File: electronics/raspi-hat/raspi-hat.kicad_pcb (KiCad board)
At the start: 0 parts

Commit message: Start laying out PCB for raspberry pi hat
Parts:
- added C1: 4.7uF, Capacitor_SMD:C_0603_1608Metric, F.Cu at (123.4, 21.1)
- added C10: 15pF, Capacitor_SMD:C_0603_1608Metric, F.Cu at (29.7, 71.3)
- added C2: 4.7uF, Capacitor_SMD:C_0603_1608Metric, F.Cu at (127.5, 21.1)
- added C3: 4.7uF, Capacitor_SMD:C_0603_1608Metric, F.Cu at (105.8, 47.5)
- added C4: 4.7uF, Capacitor_SMD:C_0603_1608Metric, F.Cu at (123.4, 23.6)
- added C5: 4.7uF, Capacitor_SMD:C_0603_1608Metric, F.Cu at (116.3, 39.4)
- added C6: HHXB350ARA680MF80G, Capacitor_SMD:CP_Elec_6.3x7.7, F.Cu at (186.2, 112.6)
- added C7: 10μF, Capacitor_SMD:C_0603_1608Metric, F.Cu at (71.4, 41.1)
- added C8: 22μF, Capacitor_SMD:C_0603_1608Metric, F.Cu at (71.4, 43.7)
- added C9: 15pF, Capacitor_SMD:C_0603_1608Metric, F.Cu at (38.2, 62.6)
- added J1: Raspberry Pi 40-Pin, Connector_PinHeader_2.54mm:PinHeader_2x20_P2.54mm_Vertical, F.Cu at (137.2, 83.8)
- added J2: 24V, Custom Footprints:PowerPoleThroughHole, F.Cu at (188.0, 82.0)
- added J3: 12V to other boards, Custom Footprints:PowerPoleThroughHole, F.Cu at (170.2, 82.0)
- added J4: CAN, Custom Footprints:LatchingConnector2POS, F.Cu at (141.0, 76.6)
- added J5: 5V to other boards, Custom Footprints:LatchingConnector2POS, F.Cu at (151.1, 76.4)
- added Q1: DMG2305UX-13, digikey-footprints:SOT-23-3, F.Cu at (35.3, 67.9)
- added R1: 10kΩ, Resistor_SMD:R_0603_1608Metric, F.Cu at (82.8, 60.7)
- added R10: 10k, Resistor_SMD:R_0603_1608Metric, F.Cu at (38.2, 60.1)
- added R2: 47kΩ, Resistor_SMD:R_0603_1608Metric, F.Cu at (71.4, 50.1)
- added R3: 330kΩ, Resistor_SMD:R_0603_1608Metric, F.Cu at (84.9, 43.7)
- added R4: 18kΩ, Resistor_SMD:R_0603_1608Metric, F.Cu at (84.9, 41.1)
- added R5: 3kΩ, Resistor_SMD:R_0603_1608Metric, F.Cu at (88.9, 41.1)
- added R6: 68Ω, Resistor_SMD:R_0603_1608Metric, F.Cu at (88.9, 43.7)
- added R7: 510kΩ, Resistor_SMD:R_0603_1608Metric, F.Cu at (75.4, 41.1)
- added R8: 100k, Resistor_SMD:R_0603_1608Metric, F.Cu at (137.3, 34.3)
- added R9: 150Ω, Resistor_SMD:R_0603_1608Metric, F.Cu at (150.0, 21.1)
- added U1: MCP2515-xSO, Package_SO:SOIC-18W_7.5x11.6mm_P1.27mm, F.Cu at (152.4, 101.6)
- added U2: MAX33012EASA+, MAX33012EASA+:MAX33012EASA+, F.Cu at (147.3, 86.4)
- added U3: DMMT5401-7-F, DMMT5401-7-F:DMMT5401-7-F, F.Cu at (121.9, 78.7)
- added U4: MYSGK02506BRSR, MYSGK02506BRSR:Murata-MYSGK-06-0-0-MFG, F.Cu at (186.7, 99.1)
- added U5: MYMGA5R04RELA5RA, MYMGA5R04RELA5RA:MYMGA5R04RELA5RA, F.Cu at (168.9, 96.5)
- added Y1: Crystal_GND24_Small, Crystal:Crystal_SMD_3225-4Pin_3.2x2.5mm, F.Cu at (58.9, 52.5)
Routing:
- net Net-(U1-Pad1): track 0.00 -> 23.3 mm
- net /SCLK: track 0.00 -> 23.0 mm, vias 0 -> 1
- net Net-(U1-Pad2): track 0.00 -> 20.4 mm
- net /CS: track 0.00 -> 17.8 mm
- net /INT: track 0.00 -> 17.5 mm, vias 0 -> 1
- net /SDO: track 0.00 -> 13.2 mm
- net /SDI: track 0.00 -> 12.7 mm
- net Net-(J4-Pad1): track 0.00 -> 9.64 mm
- net Net-(J4-Pad2): track 0.00 -> 9.12 mm
- added copper zone on F.Cu, net GND
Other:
- copper layers 0 -> 4

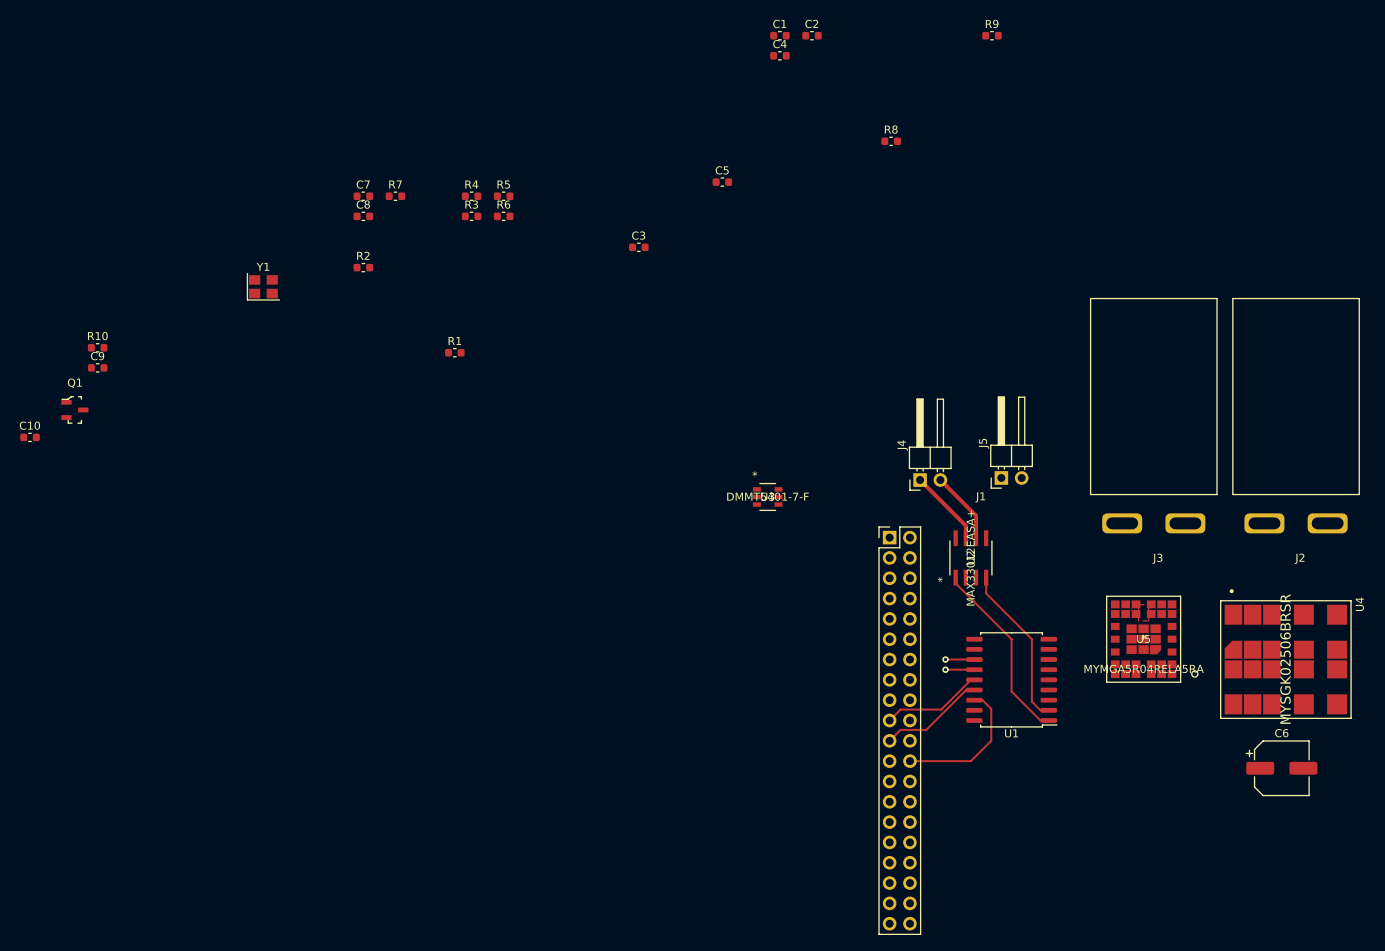
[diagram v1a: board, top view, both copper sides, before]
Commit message: Finish designing raspi hat
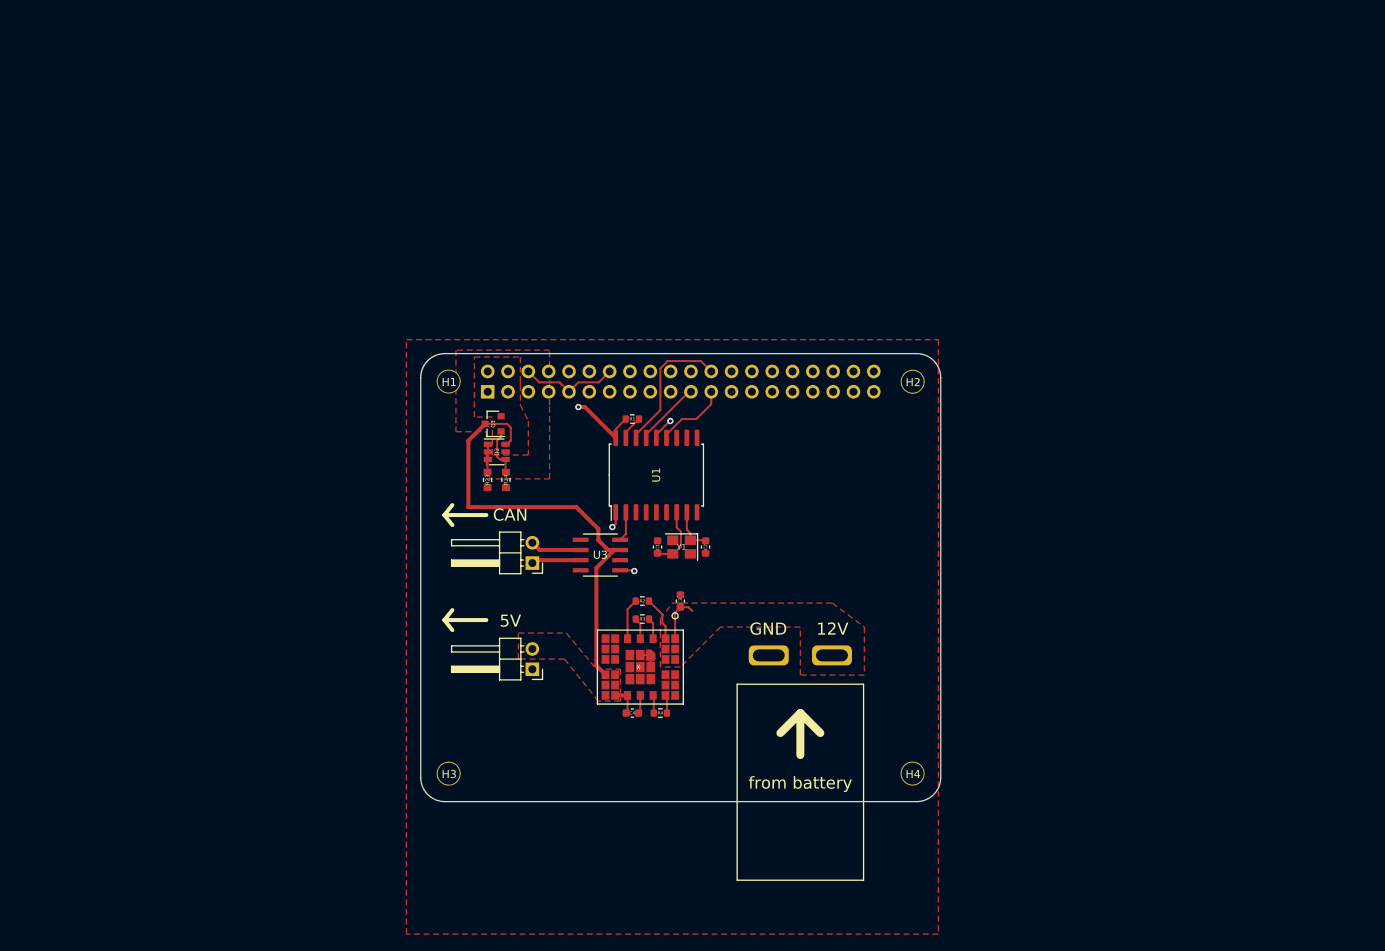
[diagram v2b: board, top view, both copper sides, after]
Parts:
- removed C10, C9: 15pF, Capacitor_SMD:C_0603_1608Metric
- removed C5: 4.7uF, Capacitor_SMD:C_0603_1608Metric
- removed C6: HHXB350ARA680MF80G, Capacitor_SMD:CP_Elec_6.3x7.7
- removed C7: 10μF, Capacitor_SMD:C_0603_1608Metric
- removed C8: 22μF, Capacitor_SMD:C_0603_1608Metric
- removed J5: 5V to other boards, Custom Footprints:LatchingConnector2POS
- removed R10: 10k, Resistor_SMD:R_0603_1608Metric
- removed R5: 3kΩ, Resistor_SMD:R_0603_1608Metric
- removed R6: 68Ω, Resistor_SMD:R_0603_1608Metric
- removed R7: 510kΩ, Resistor_SMD:R_0603_1608Metric
- removed R8: 100k, Resistor_SMD:R_0603_1608Metric
- removed R9: 150Ω, Resistor_SMD:R_0603_1608Metric
- removed U2: MAX33012EASA+, MAX33012EASA+:MAX33012EASA+
- removed U5: MYMGA5R04RELA5RA, MYMGA5R04RELA5RA:MYMGA5R04RELA5RA
- added H1: 3mm_Mounting_Hole, project_footprints:NPTH_3mm_ID, F.Cu at (82.0, 64.3)
- added H2: 3mm_Mounting_Hole, project_footprints:NPTH_3mm_ID, F.Cu at (140.0, 64.3)
- added H3: 3mm_Mounting_Hole, project_footprints:NPTH_3mm_ID, F.Cu at (82.0, 113.3)
- added H4: 3mm_Mounting_Hole, project_footprints:NPTH_3mm_ID, F.Cu at (140.0, 113.3)
- added Q2: DMMT5401, Package_TO_SOT_SMD:SOT-23-6, F.Cu at (88.0, 73.1)
- added R23: 10K, Resistor_SMD:R_0603_1608Metric_Pad0.84x1.00mm_HandSolder, F.Cu at (86.9, 76.6)
- added R24: 47K, Resistor_SMD:R_0603_1608Metric_Pad0.84x1.00mm_HandSolder, F.Cu at (89.2, 76.6)
- C1, C2: value 4.7uF -> 15pF
- C3: value 4.7uF -> 10μF
- C4: value 4.7uF -> 22μF
- J1: value Raspberry Pi 40-Pin -> 12V from battery; footprint Connector_PinHeader_2.54mm:PinHeader_2x20_P2.54mm_Vertical -> Custom Footprints:PowerPoleThroughHole
- J2: value 24V -> 5V to other boards; footprint Custom Footprints:PowerPoleThroughHole -> Custom Footprints:LatchingConnector2POS
- J3: value 12V to other boards -> 40HAT; footprint Custom Footprints:PowerPoleThroughHole -> Connector_PinSocket_2.54mm:PinSocket_2x20_P2.54mm_Vertical; moved to B.Cu
- Q1: value DMG2305UX-13 -> DMG2305UX; footprint digikey-footprints:SOT-23-3 -> Package_TO_SOT_SMD:SOT-23
- R1: value 10kΩ -> 10k
- R2: value 47kΩ -> 510kΩ
- R3: value 330kΩ -> 100k
- R4: value 18kΩ -> 150Ω
- U3: value DMMT5401-7-F -> MAX33012EASA+; footprint DMMT5401-7-F:DMMT5401-7-F -> MAX33012EASA+:MAX33012EASA+
- U4: value MYSGK02506BRSR -> MYMGA5R04RELA5RA; footprint MYSGK02506BRSR:Murata-MYSGK-06-0-0-MFG -> MYMGA5R04RELA5RA:MYMGA5R04RELA5RA
- moved J2 97.2 mm to (92.5, 100.3), turned to 180 degrees
- moved J3 84.9 mm to (86.9, 65.6), turned to -90 degrees
- moved C4 84.2 mm to (105.0, 105.8), turned to 180 degrees
- moved U4 80.7 mm to (106.0, 100.0)
- moved R4 68.8 mm to (108.5, 105.8), turned to 180 degrees
- moved C1 65.7 mm to (108.2, 85.0), turned to -90 degrees
- moved C2 65.3 mm to (114.2, 85.0), turned to 90 degrees
- moved Y1 61.6 mm to (111.2, 85.0), turned to 180 degrees
- moved R3 54.7 mm to (106.2, 94.0), turned to 180 degrees
- moved R2 54.3 mm to (106.2, 91.8)
- moved Q1 52.3 mm to (87.6, 69.6), turned to 180 degrees
- moved U1 51.3 mm to (108.0, 76.0), turned to 90 degrees
- moved J4 49.6 mm to (92.5, 87.0), turned to 180 degrees
- moved C3 44.5 mm to (111.0, 91.8), turned to 90 degrees
- moved R1 23.7 mm to (105.0, 69.0), turned to 180 degrees
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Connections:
- C1 pad 1: +24V -> GND
- C1 pad 2: GND -> Net-(C1-Pad2)
- C2 pad 1: +24V -> GND
- C2 pad 2: GND -> Net-(C2-Pad2)
- C3 pad 1: +24V -> +12V
- C4 pad 1: +24V -> GND
- C4 pad 2: GND -> +5V
- J1 pad 1: /3v3 -> GND
- J1 pad 2: /5VP -> +12V
- J2 pad 1: +24V -> GND
- J2 pad 2: GND -> +5V
- J3 pad 1: GND -> /P3V3_HAT
- J3 pad 2: +12V -> /P5V_HAT
- Q1 pad 2: /5VP -> /P5V_HAT
- R1 pad 2: GND -> /P3V3_HAT
- R2 pad 1: Net-(Q1-Pad1) -> Net-(R2-Pad1)
- R2 pad 2: GND -> +12V
- R3 pad 1: +24V -> Net-(R3-Pad1)
- R4 pad 1: Net-(R3-Pad2) -> GND
- R4 pad 2: GND -> Net-(R4-Pad2)
- U1 pad 17: Net-(R10-Pad1) -> Net-(R1-Pad1)
- U1 pad 18: +3V3 -> /P3V3_HAT
- U1 pad 7: Net-(C9-Pad2) -> Net-(C1-Pad2)
- U1 pad 8: Net-(C10-Pad2) -> Net-(C2-Pad2)
- U3 pad 1: Net-(Q1-Pad1) -> Net-(U1-Pad1)
- U3 pad 2: Net-(R1-Pad1) -> GND
- U3 pad 3: Net-(R1-Pad1) -> +5V
- U3 pad 4: Net-(R1-Pad1) -> Net-(U1-Pad2)
- U3 pad 5: +5V -> unconnected-(U3-Pad5)
- U3 pad 6: /5VP -> Net-(J4-Pad2)
- U4 pad 1: +24V -> +12V
- U4 pad 10: +12V -> GND
- U4 pad 11: +12V -> GND
- U4 pad 12: +12V -> GND
- U4 pad 14: Net-(R5-Pad1) -> GND
- U4 pad 16: GND -> +5V
- U4 pad 17: Net-(R3-Pad2) -> +5V
- U4 pad 18: GND -> +5V
- U4 pad 19: GND -> +5V
- U4 pad 2: +24V -> +12V
- U4 pad 20: GND -> +5V
- U4 pad 3: +24V -> +12V
- U4 pad 4: GND -> +12V
- U4 pad 5: GND -> +12V
- U4 pad 6: GND -> +12V
- U4 pad 7: GND -> Net-(R3-Pad1)
- U4 pad 8: GND -> Net-(R3-Pad2)
- U4 pad 9: GND -> Net-(R2-Pad1)
- Y1 pad 1: Net-(C10-Pad2) -> Net-(C2-Pad2)
- Y1 pad 3: Net-(C9-Pad2) -> Net-(C1-Pad2)
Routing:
- net +5V: track 0.00 -> 61.0 mm
- net /P3V3_HAT: track 0.00 -> 21.3 mm, vias 0 -> 1
- net GND: track 0.08 -> 19.6 mm
- net /INT: track 17.5 -> 0.00 mm, vias 1 -> 0
- net Net-(U1-Pad2): track 20.4 -> 3.75 mm
- net /SCLK: track 23.0 -> 9.13 mm, vias 1 -> 0
- net Net-(U1-Pad1): track 23.3 -> 10.5 mm, vias 0 -> 2
- net +12V: track 0.00 -> 11.5 mm
- net Net-(C1-Pad2): track 0.00 -> 8.40 mm
- net /SDI: track 12.7 -> 6.54 mm, vias 0 -> 1
- net Net-(Q1-Pad1): track 0.00 -> 6.02 mm
- net Net-(C2-Pad2): track 0.00 -> 6.01 mm
- net Net-(R2-Pad1): track 0.00 -> 5.13 mm
- net /SDO: track 13.2 -> 8.23 mm
- net Net-(J4-Pad1): track 9.64 -> 6.19 mm
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- added copper zone on F.Cu, net +12V
- added copper zone on F.Cu, net +5V
- added copper zone on F.Cu, net /P5V_HAT
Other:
- board outline added: 65 x 56 mm
- board text added: "12V"
- board text added: "5V"
- board text added: "CAN"
- board text added: "GND"
- board text added: "If you want to use an SMT 40-pin header, please move the top edge up by 0.5mm and locate the header in the same location as the current TH part."
- board text added: "This is a HAT compatible PCB starting design based on the official Raspberry Pi specs at: https://github.com/raspberrypi/hats/blob/master/designguide.md Currently the camera slot and display cutout are not here. See the schematic for the details on the EEPROM and power setup. This board does have the correct components for powering the Pi via the HAT. If you need the Pi to provide 5V or 3.3V, ple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"
- board text added: "from battery"

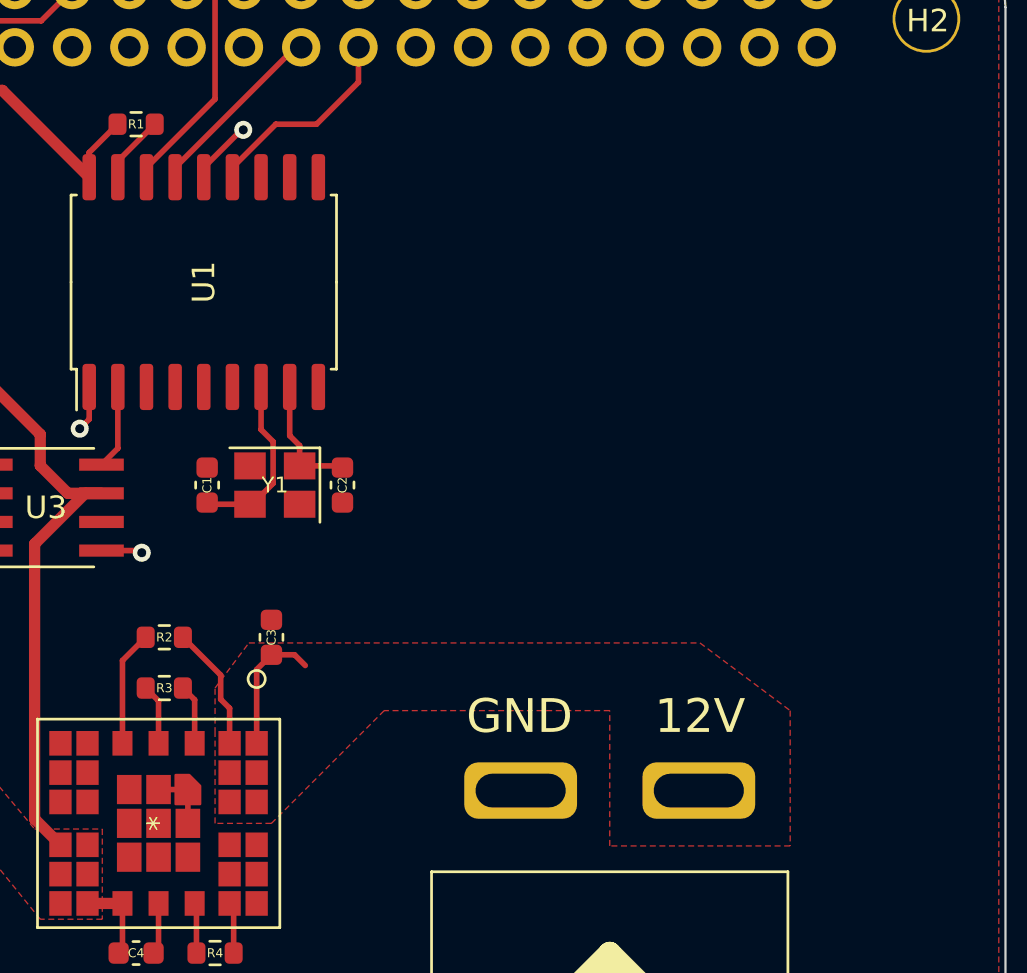
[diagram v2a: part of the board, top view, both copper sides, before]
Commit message: Add SEDS logo to raspberry pi hat
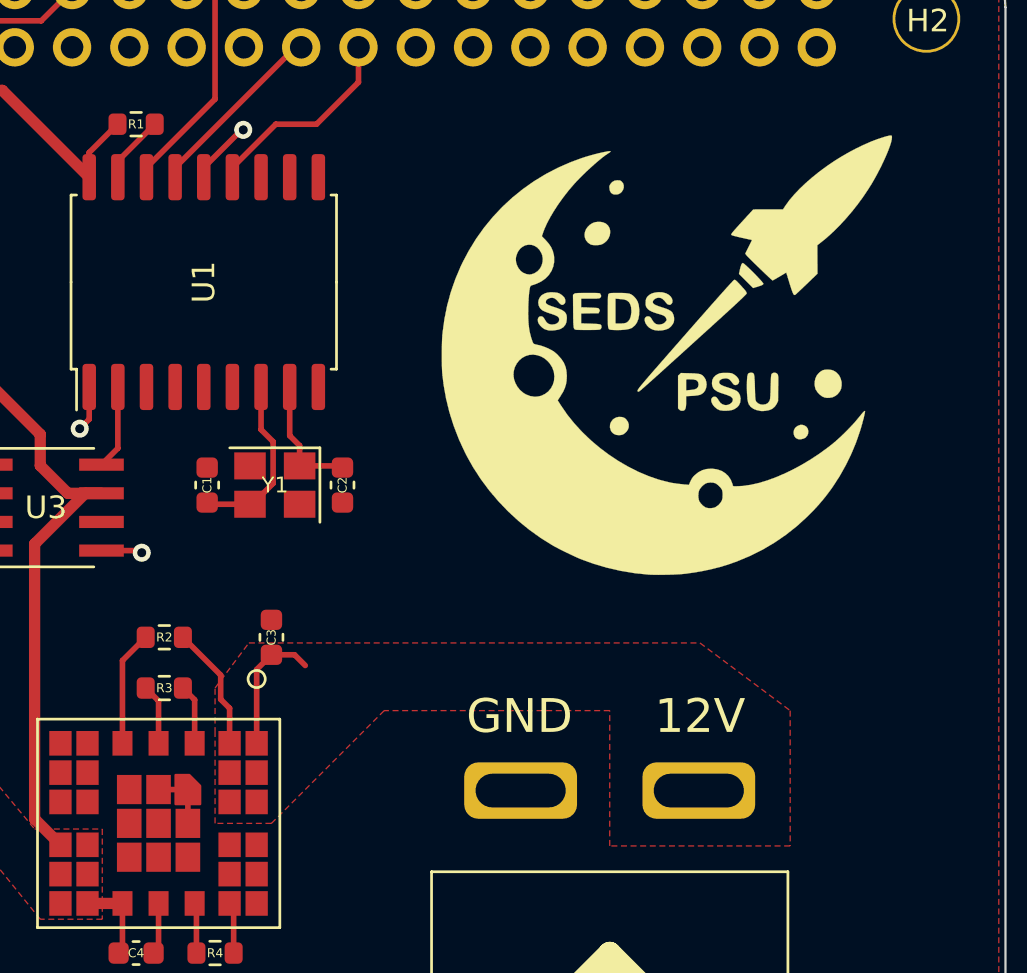
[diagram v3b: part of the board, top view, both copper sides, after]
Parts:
- added Ref**: Val**, Custom Footprints:seds-logo, F.Cu at (128.5, 79.0)
